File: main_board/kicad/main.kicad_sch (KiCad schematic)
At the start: 14 parts, among them J1 Sensorbuchse, J2 Motorbuchse, J3 Motorbuchse, J4 Batteriebuchse, J5 Conn_02x07_Odd_Even, J6 Sensorbuchse, J7 AVR-ISP-10

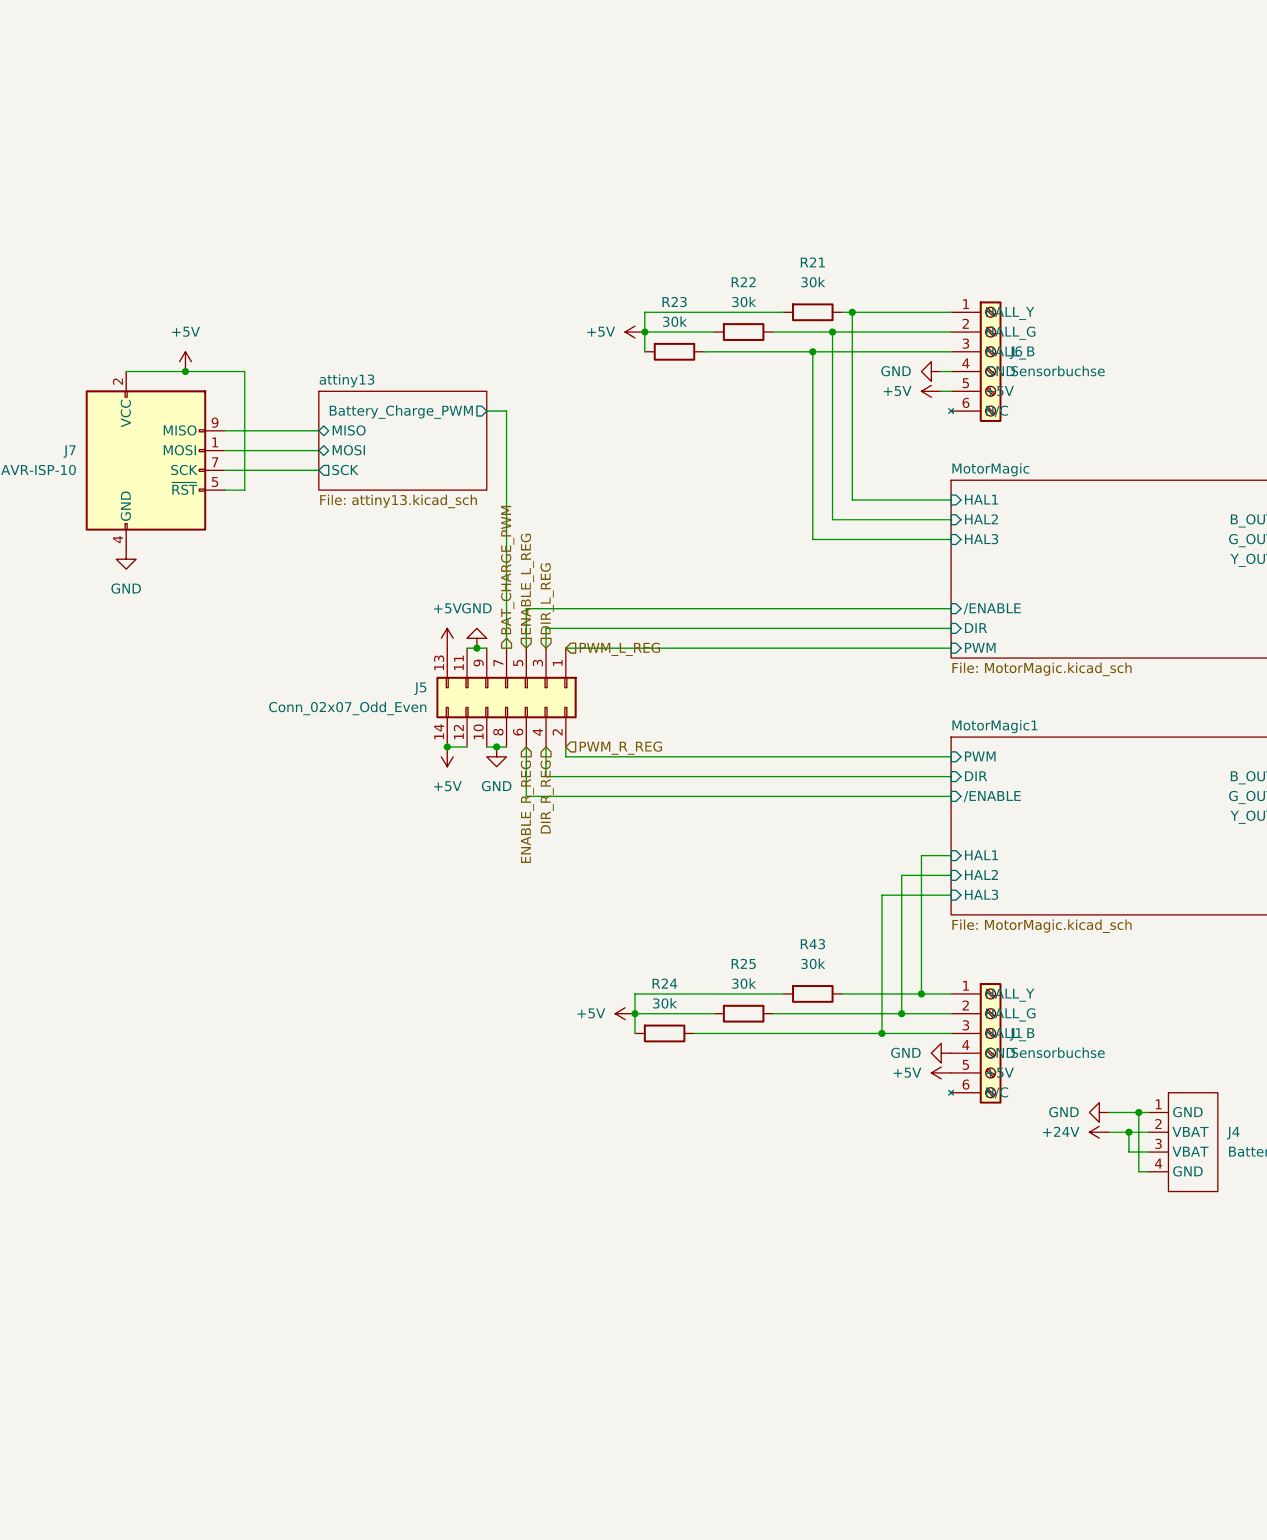
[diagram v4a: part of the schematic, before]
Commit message: added LEDS and fuses
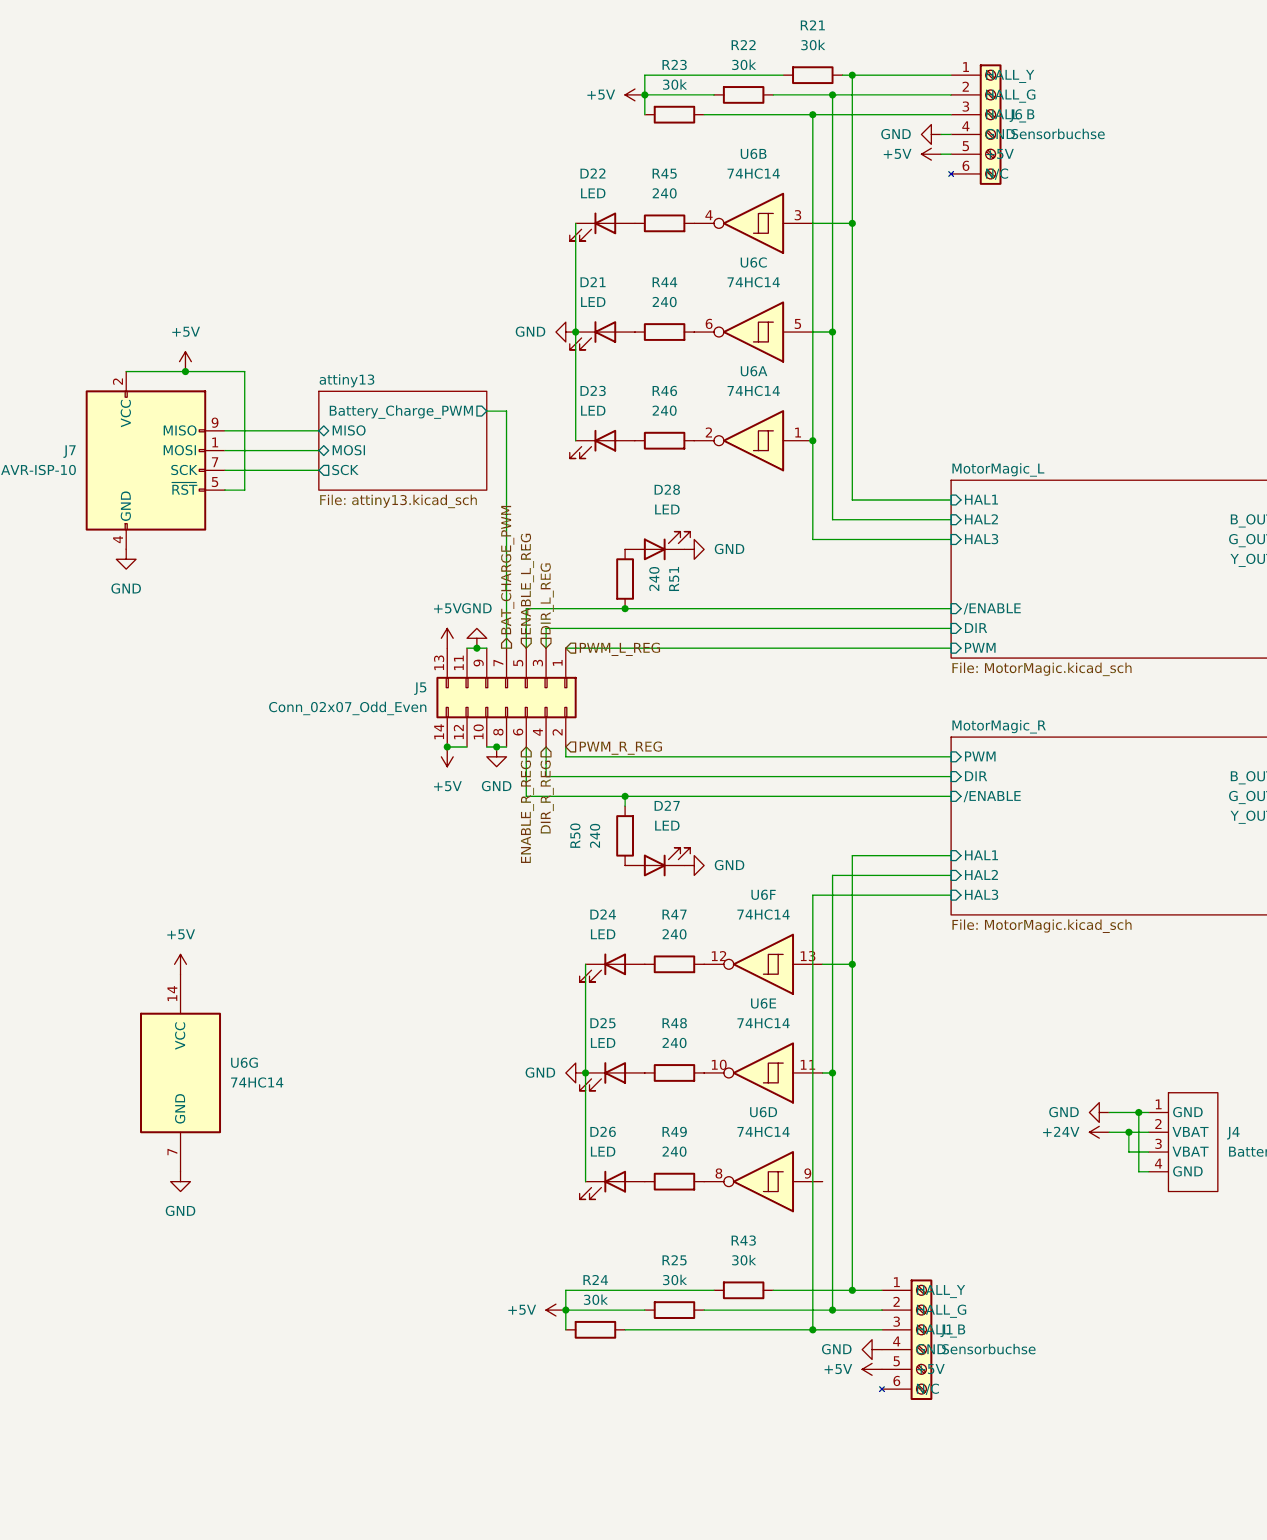
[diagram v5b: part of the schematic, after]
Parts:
- added D21, D22, D23, D24, D25, D26, D27, D28: LED, symbol Device:LED
- added R44, R45, R46, R47, R48, R49, R50, R51: 240, symbol Device:R
- added U6: 74HC14, symbol 74xx:74HC14
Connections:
- net +5V: now also U6.14 (VCC)
- net ENABLE_L_REG: now also R51.2
- net ENABLE_R_REG: now also R50.2
- net GND: now also D21.1 (K), D22.1 (K), D23.1 (K), D24.1 (K), D25.1 (K), D26.1 (K), D27.1 (K), D28.1 (K), U6.7 (GND)
- net MotorMagic_L/HAL1: now also U6.3
- net MotorMagic_L/HAL2: now also U6.5
- net MotorMagic_L/HAL3: now also U6.1
- net MotorMagic_R/HAL1: now also U6.13
- net MotorMagic_R/HAL2: now also U6.11
- new net: D24.2 (A), R47.1
- new net: R47.2, U6.12
- new net: D22.2 (A), R45.1
- new net: D28.2 (A), R51.1
- new net: D26.2 (A), R49.1
- new net: R49.2, U6.8
- new net: D23.2 (A), R46.1
- new net: R46.2, U6.2
- new net: R45.2, U6.4
- new net: R44.2, U6.6
- new net: D25.2 (A), R48.1
- new net: D21.2 (A), R44.1
- new net: D27.2 (A), R50.1
- new net: R48.2, U6.10
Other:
- sheet MotorMagic renamed MotorMagic_L
- sheet MotorMagic1 renamed MotorMagic_R
- moved on the sheet: J1, J6, R21, R22, R23, R24, R25, R43

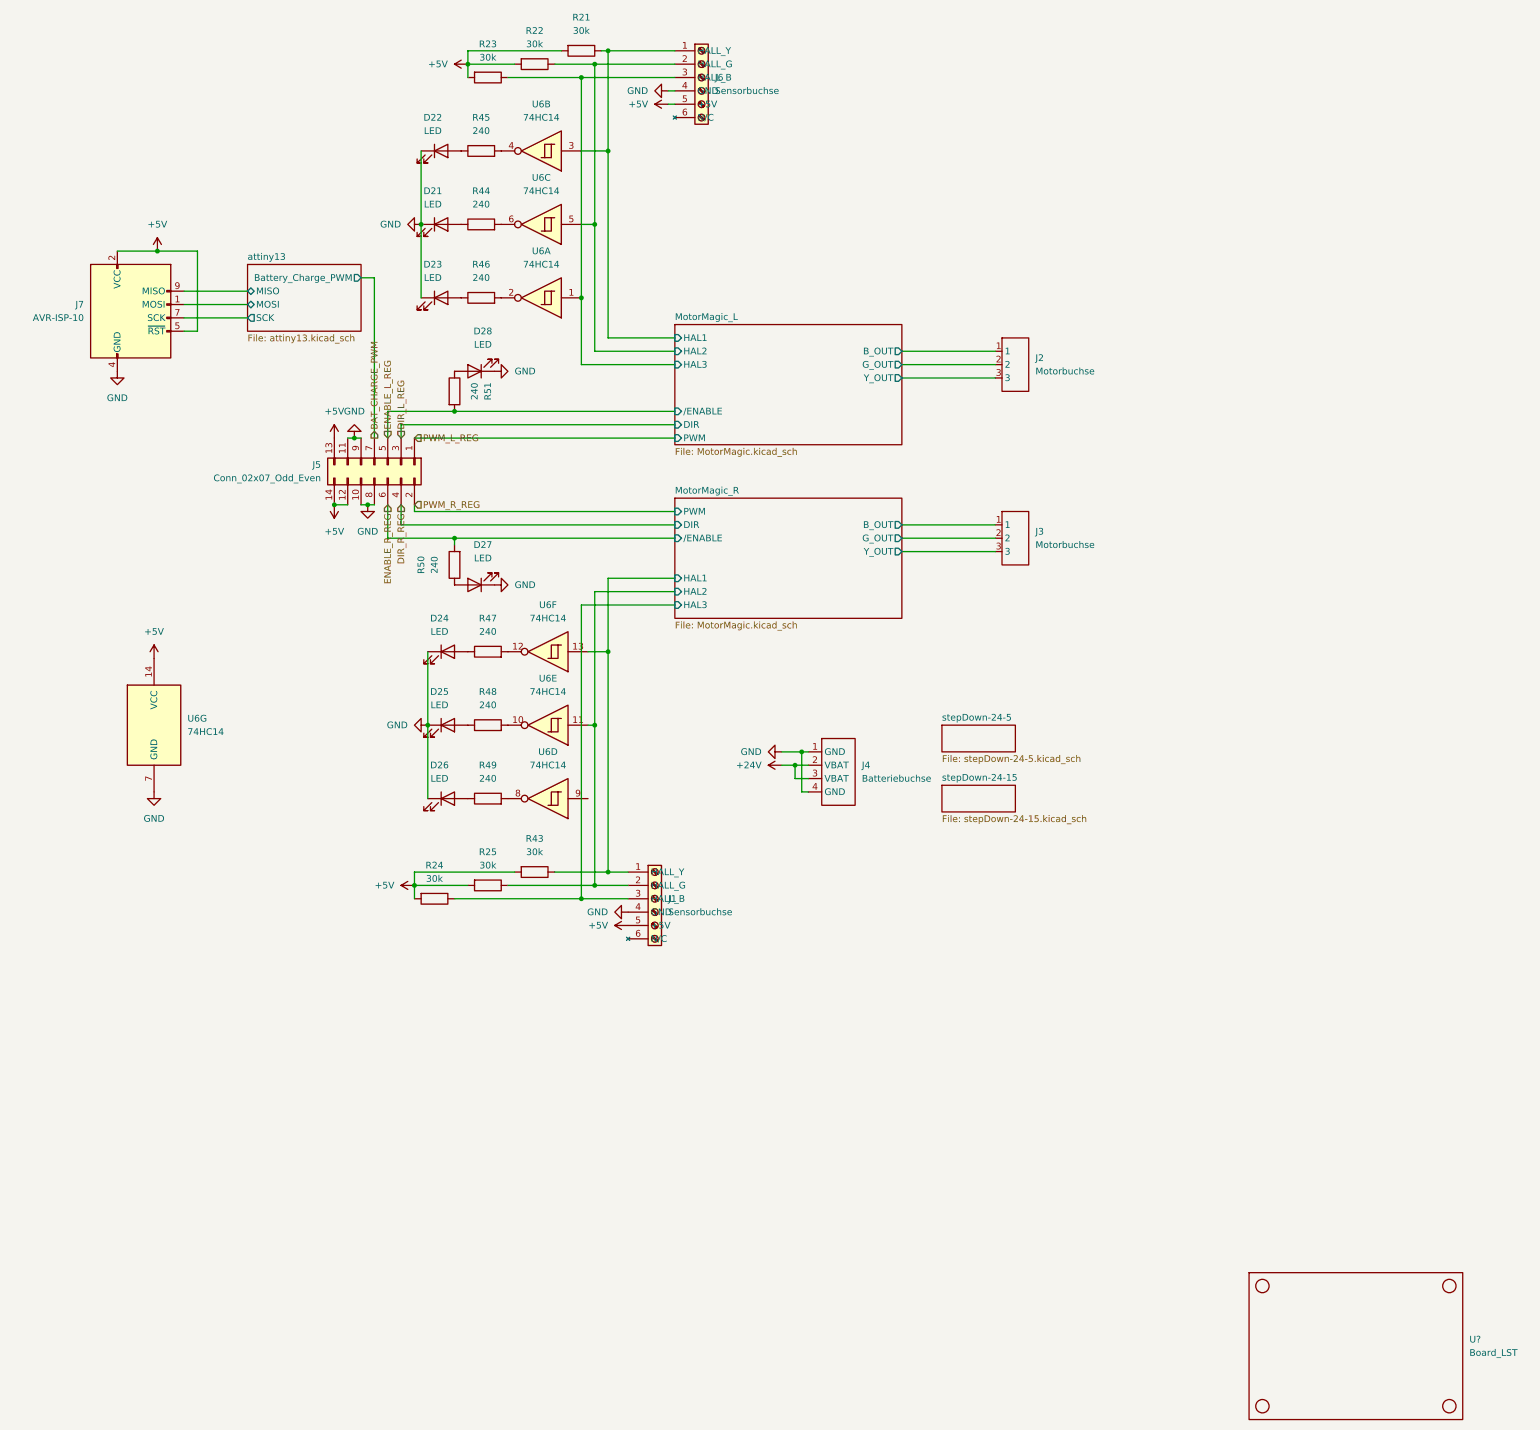
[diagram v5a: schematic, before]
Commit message: resolved ERC
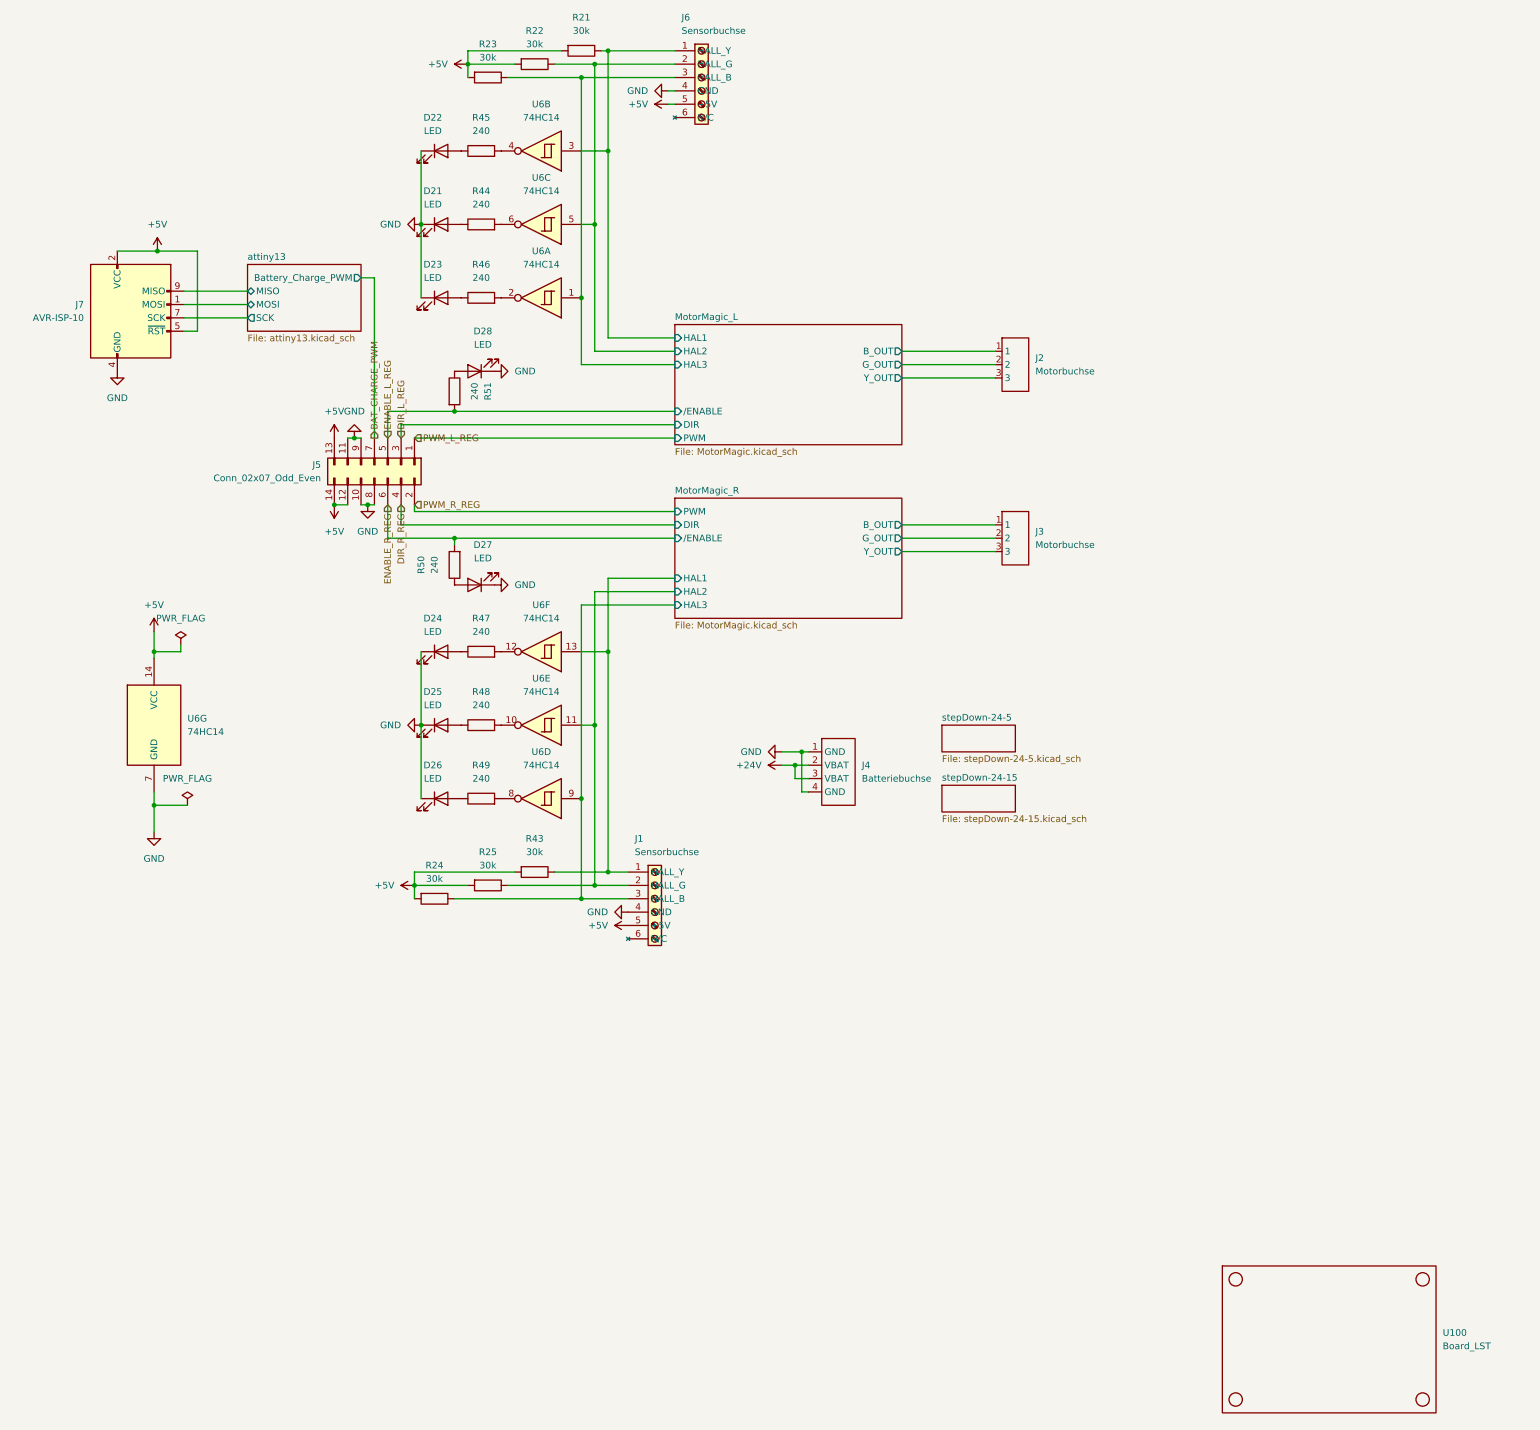
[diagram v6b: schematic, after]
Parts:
- gave numbers to parts that had none: 1
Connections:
- net MotorMagic_R/HAL3: now also U6.9
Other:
- moved on the sheet: D24, D25, D26, R47, R48, R49, U100, U6D, U6E, U6F

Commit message: updated to post review state
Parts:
- removed R43: 30k, symbol Device:R
- added C32: 100nF, symbol Device:C
- added R20: 3k, symbol Device:R
- R21, R22, R23, R24, R25: value 30k -> 3k
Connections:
- net +5V: now also R50.2, R51.2, C32.1, R20.2; no longer J7.5 (~{RST})
- net ENABLE_L_REG: now also D28.1 (K); no longer R51.2
- net ENABLE_R_REG: now also D27.1 (K); no longer R50.2
- net GND: no longer D27.1 (K), D28.1 (K)
- net MotorMagic_L/HAL2: now also R20.1; no longer R22.1
- net MotorMagic_L/HAL3: now also R22.1; no longer R23.1
- net MotorMagic_R/HAL1: now also R25.1
- net MotorMagic_R/HAL2: now also R24.1; no longer R25.1
- net MotorMagic_R/HAL3: now also R23.1; no longer R24.1
- new net attiny13//RESET: J7.5 (~{RST})
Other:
- sheet attiny13 ports: added /RESET; removed none
- moved on the sheet: D27, D28, J7, R50, R51

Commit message: corrected issues detected in review
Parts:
- added D29, D30: LED, symbol Device:LED
- added R52, R53: 240, symbol Device:R
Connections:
- net DIR_L_REG: now also R53.1
- net DIR_R_REG: now also R52.2
- net GND: now also C32.2, D29.1 (K), D30.1 (K)
- new net: D30.2 (A), R53.2
- new net: D29.2 (A), R52.1
